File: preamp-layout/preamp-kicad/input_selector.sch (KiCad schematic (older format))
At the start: 40 parts, among them J51 Conn_01x03_Female, J52 Conn_01x03_Male, J53 Conn_01x03_Male, J54 Conn_01x03_Male, J55 Conn_01x03_Male, J56 Conn_01x07_Female, J57 Conn_01x07_Female, J58 Conn_01x03_Male, J59 Conn_01x03_Male, J60 Conn_01x03_Female, J61 Conn_01x02_Female, J62 Conn_01x02_Male, J63 Conn_01x03_Female, J64 Conn_01x03_Female, K1 G6JU, K2 G6JU, K3 G6JU, K4 G6JU, K5 G6JU, K6 G6JU, K7 G6JU, U10 ULN2003, U11 ULN2003, U9 MCP23S17_SP

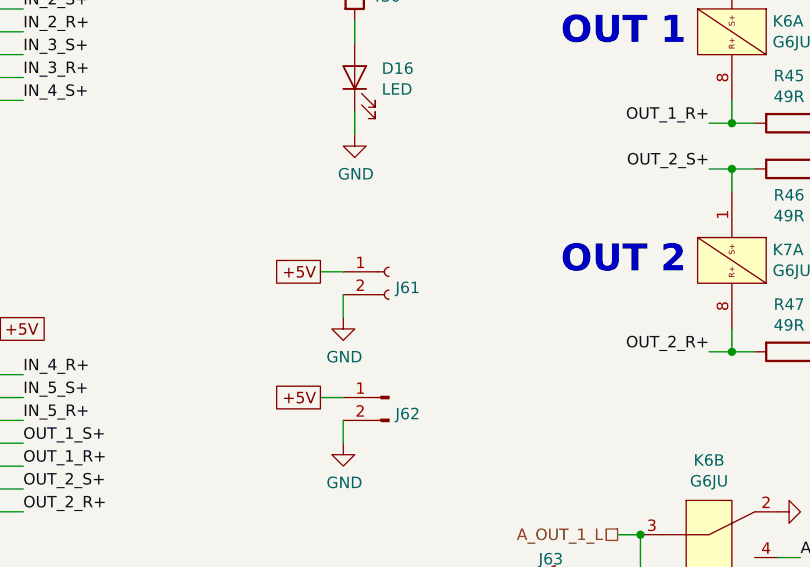
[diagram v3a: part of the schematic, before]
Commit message: power headers updated, slight BOM update
changed footprint on all 5V, +-15V to JST B2B / B3B connectors. All male conns now.
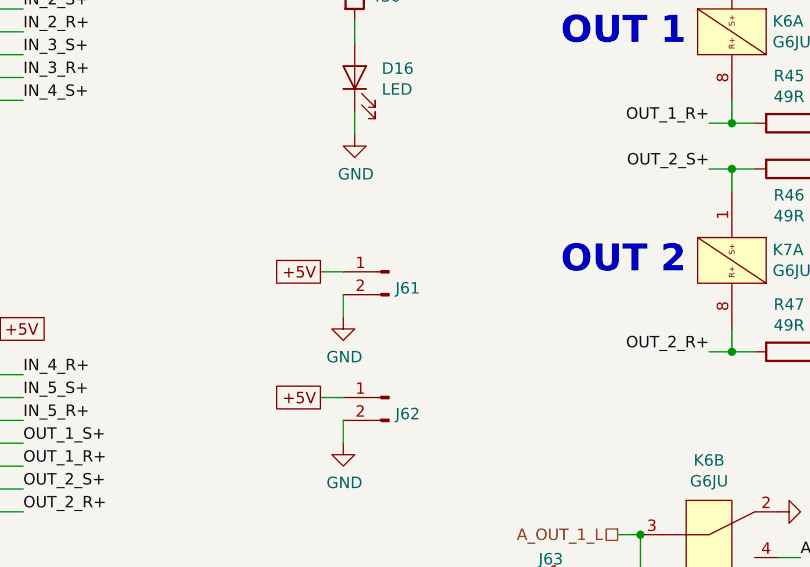
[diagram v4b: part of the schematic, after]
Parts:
- removed J61: Conn_01x02_Female, Connector_PinHeader_2.54mm:PinHeader_1x02_P2.54mm_Vertical, symbol Connector:Conn_01x02_Female
- added J61: Conn_01x02_Male, Connector_JST:JST_EH_B2B-EH-A_1x02_P2.50mm_Vertical, symbol Connector:Conn_01x02_Male
- J62: footprint Connector_PinHeader_2.54mm:PinHeader_1x02_P2.54mm_Vertical -> Connector_JST:JST_EH_B2B-EH-A_1x02_P2.50mm_Vertical
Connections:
- net +5V: now also J61.1 (Pin_1)
- net GND: now also J61.2 (Pin_2)
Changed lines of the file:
@@
 Text GLabel 6850 2750 0    50   UnSpc ~ 0
 +5V
-$Comp
-L Connector:Conn_01x02_Female J61
-U 1 1 638B3B3E
-P 7150 2750
-F 0 "J61" H 7178 2680 50  0000 L CNN
-F 1 "Conn_01x02_Female" H 7178 2635 50  0001 L CNN
-F 2 "Connector_PinHeader_2.54mm:PinHeader_1x02_P2.54mm_Vertical" H 7150 2750 50  0001 C CNN
-F 3 "~" H 7150 2750 50  0001 C CNN
-	1    7150 2750
-	1    0    0    -1
-$EndComp
 Text Label 5550 3800 0    50   ~ 0
 OUT_2_R+
@@
 F 0 "J62" H 7122 3228 50  0000 R CNN
 F 1 "Conn_01x02_Male" H 7122 3183 50  0001 R CNN
-F 2 "Connector_PinHeader_2.54mm:PinHeader_1x02_P2.54mm_Vertical" H 7150 3300 50  0001 C CNN
+F 2 "Connector_JST:JST_EH_B2B-EH-A_1x02_P2.50mm_Vertical" H 7150 3300 50  0001 C CNN
 F 3 "~" H 7150 3300 50  0001 C CNN
 	1    7150 3300
@@
 	0    1    1    0
 $EndComp
+$Comp
+L Connector:Conn_01x02_Male J61
+U 1 1 5E5DB820
+P 7150 2750
+F 0 "J61" H 7122 2678 50  0000 R CNN
+F 1 "Conn_01x02_Male" H 7122 2633 50  0001 R CNN
+F 2 "Connector_JST:JST_EH_B2B-EH-A_1x02_P2.50mm_Vertical" H 7150 2750 50  0001 C CNN
+F 3 "~" H 7150 2750 50  0001 C CNN
+	1    7150 2750
+	-1   0    0    -1
+$EndComp
 $EndSCHEMATC

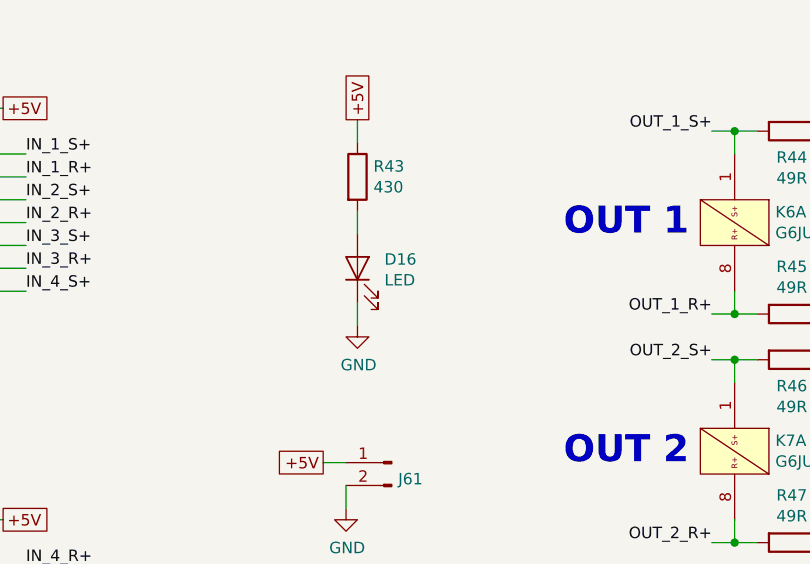
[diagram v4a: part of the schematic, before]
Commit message: Added front panel LED sheet. BOM update. Front panel PCA work
other minor changes like LED color assignments, etc
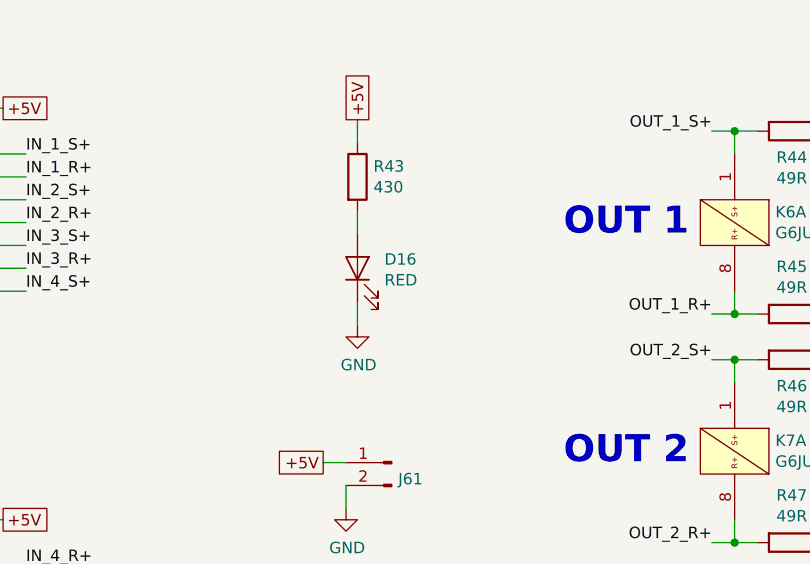
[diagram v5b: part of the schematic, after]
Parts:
- D16: value LED -> RED
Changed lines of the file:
@@
 $Descr A4 11693 8268
 encoding utf-8
-Sheet 10 11
+Sheet 10 12
 Title "IO Relay Select Board"
 Date "2020-01-23"
@@
 P 7000 1900
 F 0 "D16" V 7039 1782 50  0000 R CNN
-F 1 "LED" V 6948 1782 50  0000 R CNN
+F 1 "RED" V 6948 1782 50  0000 R CNN
 F 2 "LED_SMD:LED_1206_3216Metric_Pad1.42x1.75mm_HandSolder" H 7000 1900 50  0001 C CNN
 F 3 "~" H 7000 1900 50  0001 C CNN

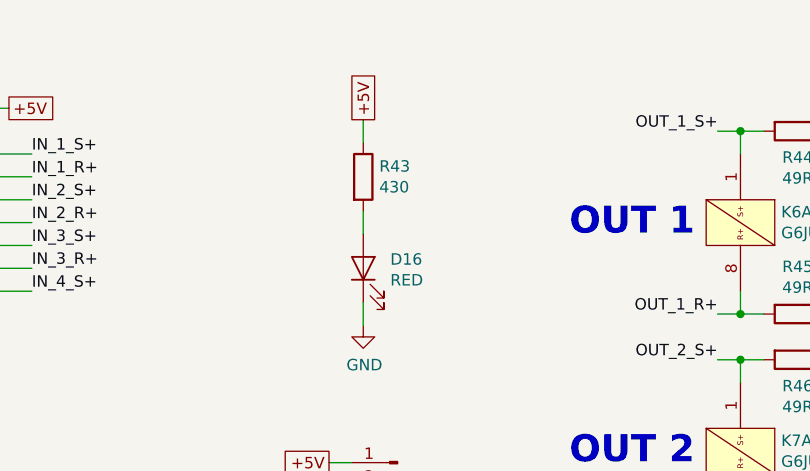
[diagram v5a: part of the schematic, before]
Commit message: LED resistor update
In the process of reviewing layouts and associated parts sourcing, I realized that I had incorrectly calculated the resistors needed for the power supply LEDs on all boards. Updated BOM and schematics to match. Other minor schematic updates.
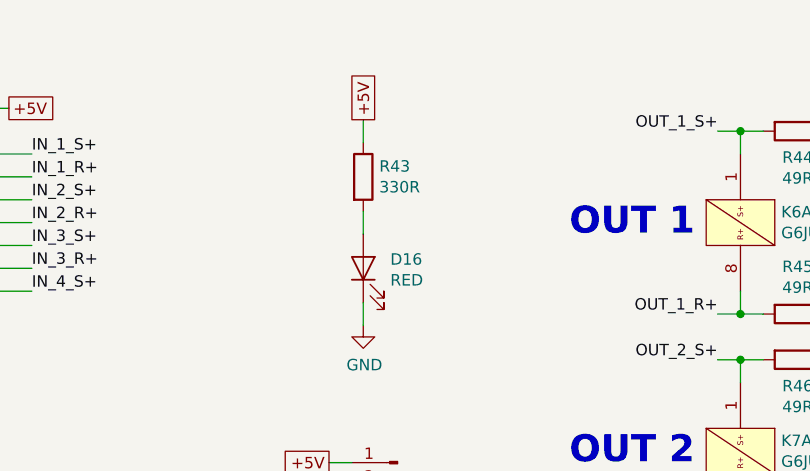
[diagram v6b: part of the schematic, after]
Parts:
- R43: value 430 -> 330R
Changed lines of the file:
@@
 AR Path="/5FDEBED2" Ref="R?"  Part="1"
 F 0 "R43" H 7070 1546 50  0000 L CNN
-F 1 "430" H 7070 1455 50  0000 L CNN
+F 1 "330R" H 7070 1455 50  0000 L CNN
 F 2 "Resistor_SMD:R_1206_3216Metric_Pad1.42x1.75mm_HandSolder" V 6930 1500 50  0001 C CNN
 F 3 "~" H 7000 1500 50  0001 C CNN

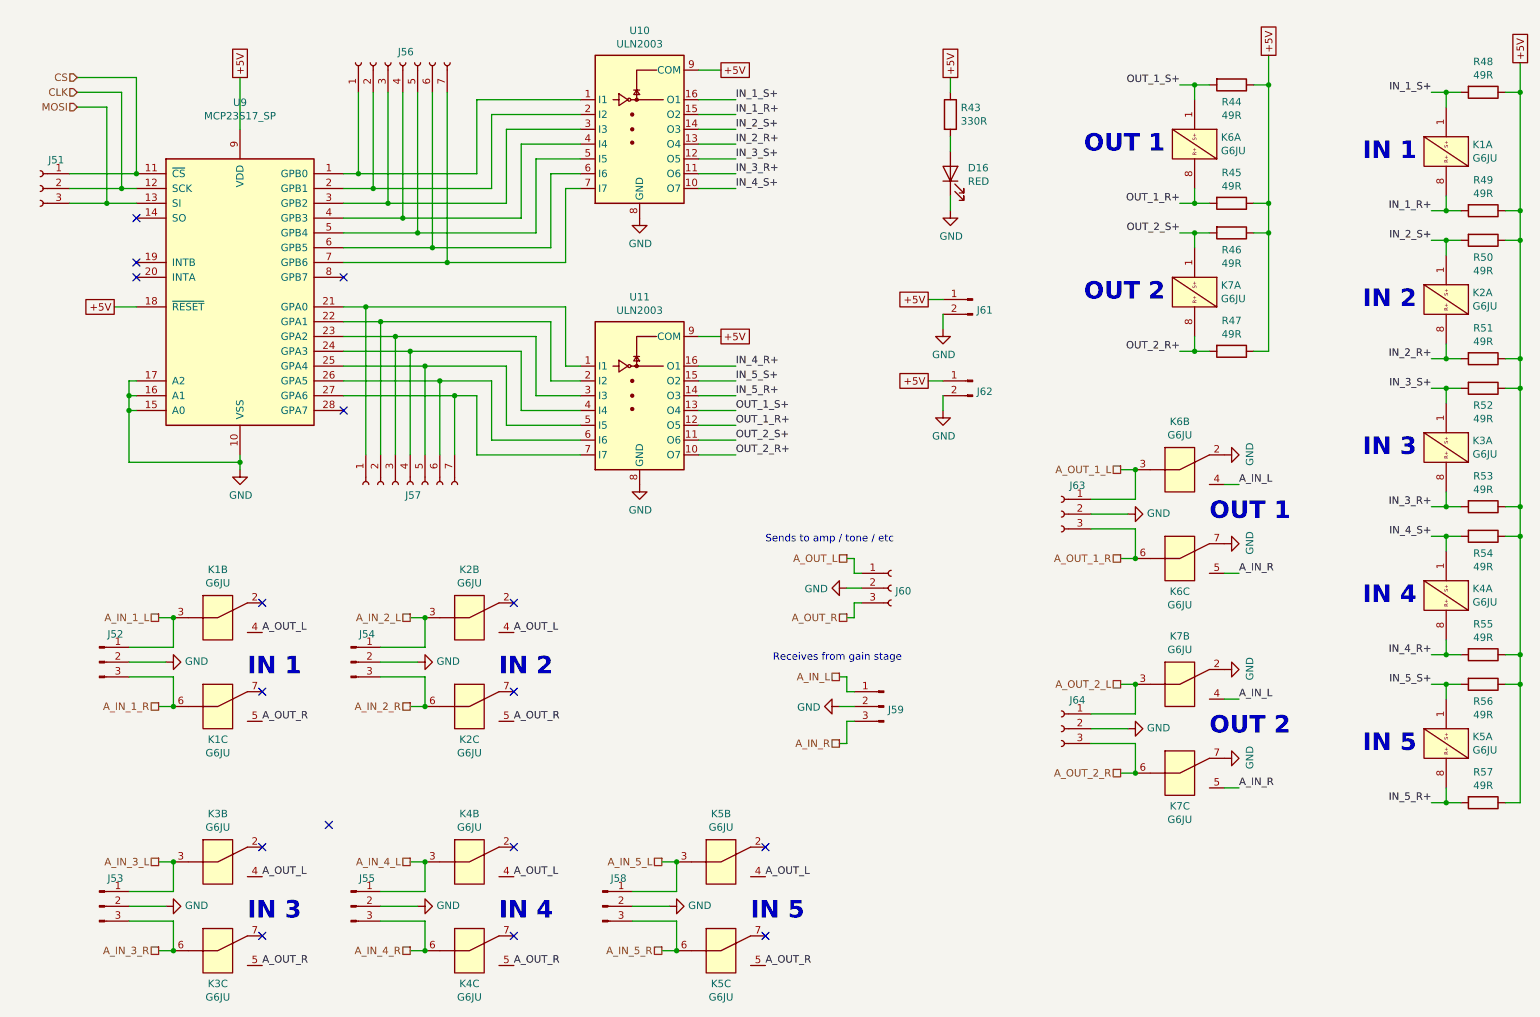
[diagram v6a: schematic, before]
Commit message: Initial Review
Reviewing schematic, comparing to references and filling in BOM to match schematics. Updating footprints in the process as well.
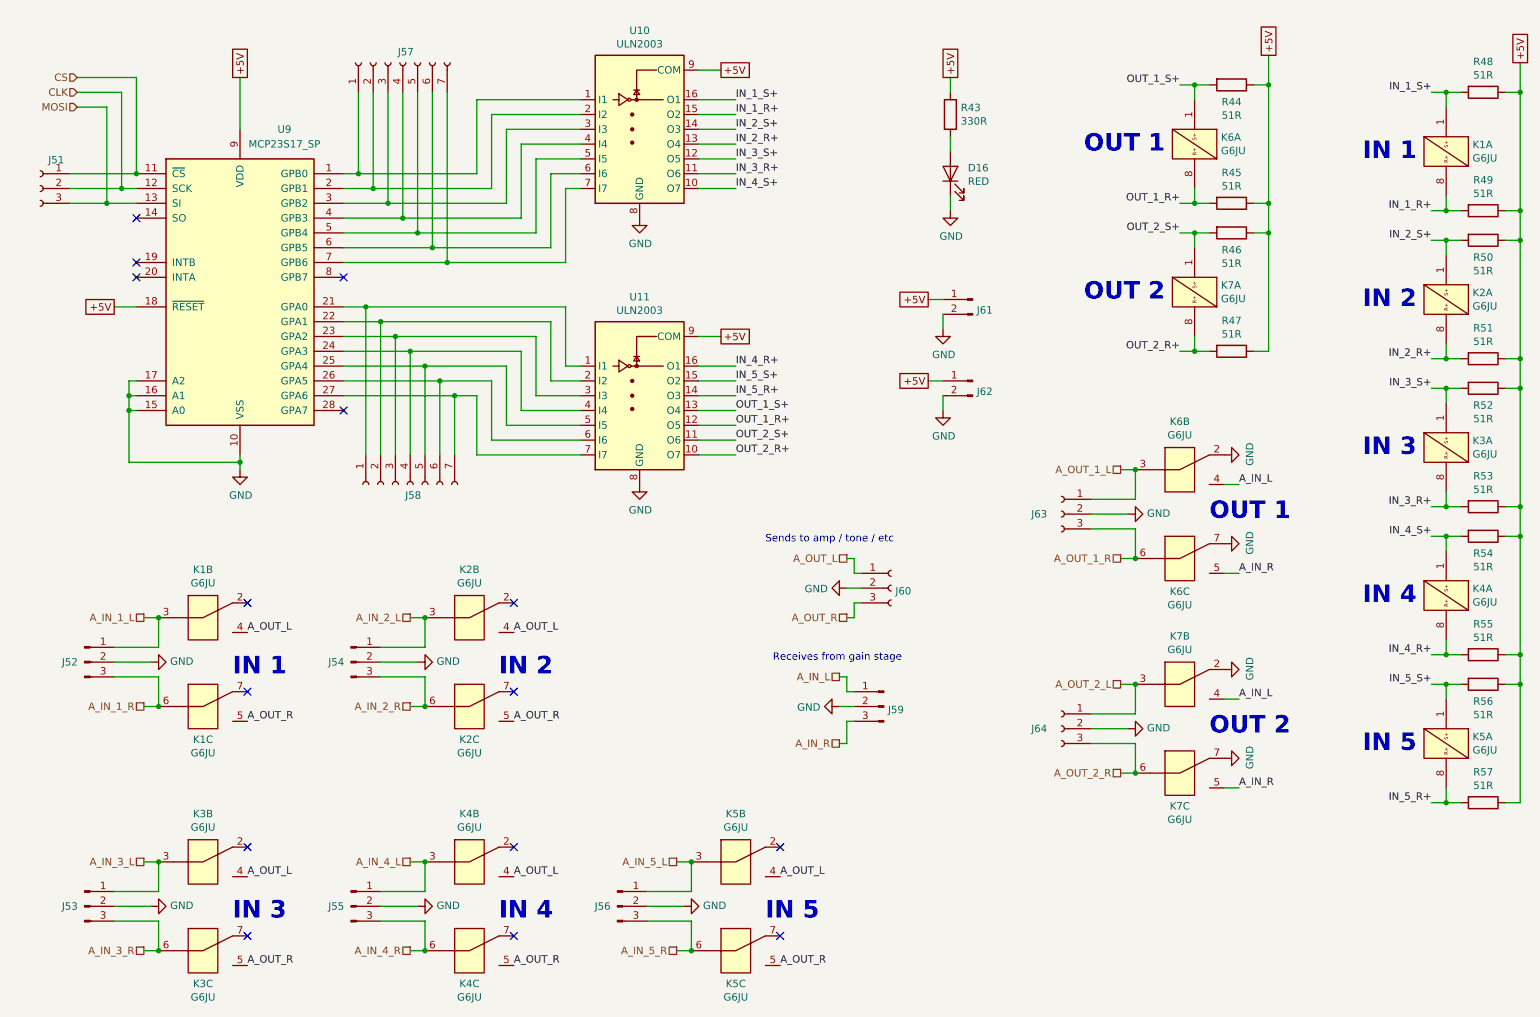
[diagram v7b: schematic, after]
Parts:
- R44, R45, R46, R47, R48, R49, R50, R51, R52, R53, R54, R55, R56, R57: value 49R -> 51R
- renumbered J58 to J56, J56 to J57, J57 to J58
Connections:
- no-connect marks 16 -> 15
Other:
- moved on the sheet: J52, J53, J56, K1B, K1C, K3B, K3C, K5B, K5C
